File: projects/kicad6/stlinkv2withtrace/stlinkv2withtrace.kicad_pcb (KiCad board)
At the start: 2 copper layers, 7 parts, among them J1 5v jumper, J2 Trace Jumper, J3 STLinkV2, U1 YAAJ_BluePill_Part_Like

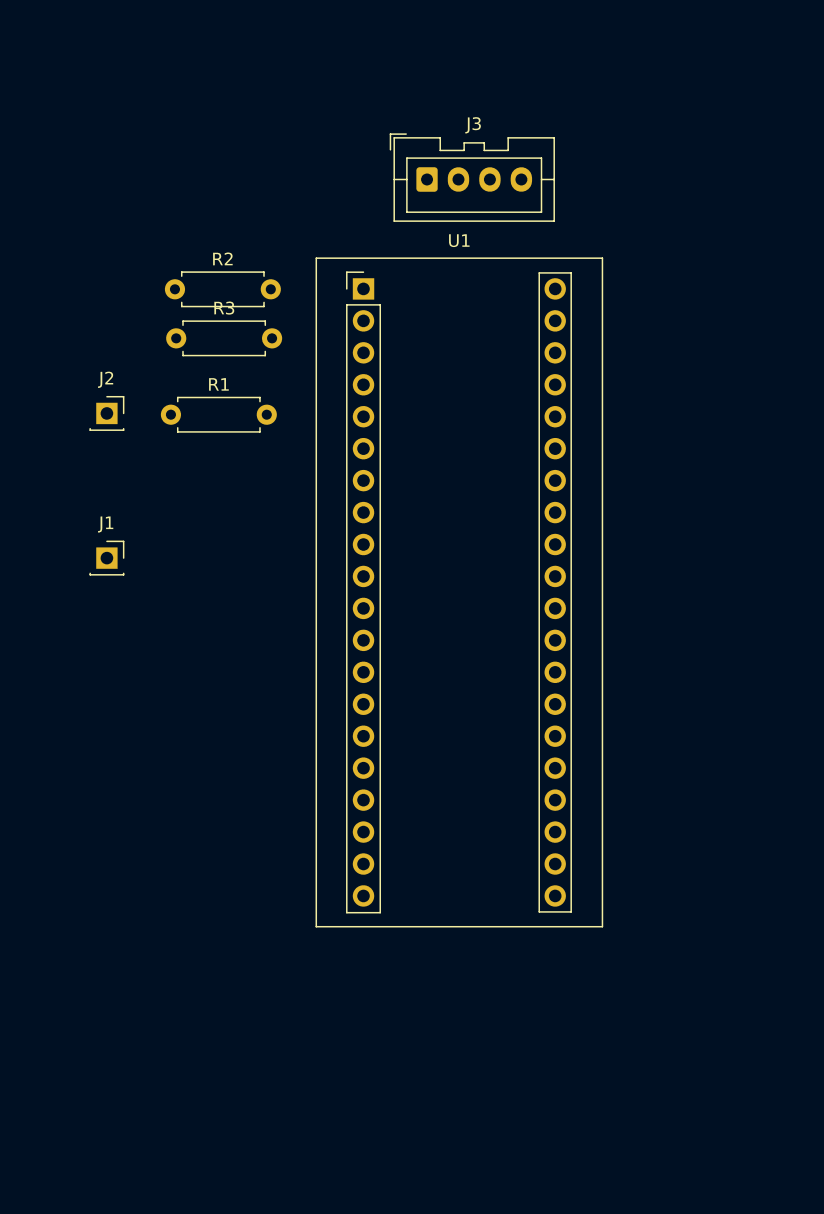
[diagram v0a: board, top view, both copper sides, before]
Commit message: Add stlink v2 diy programmer
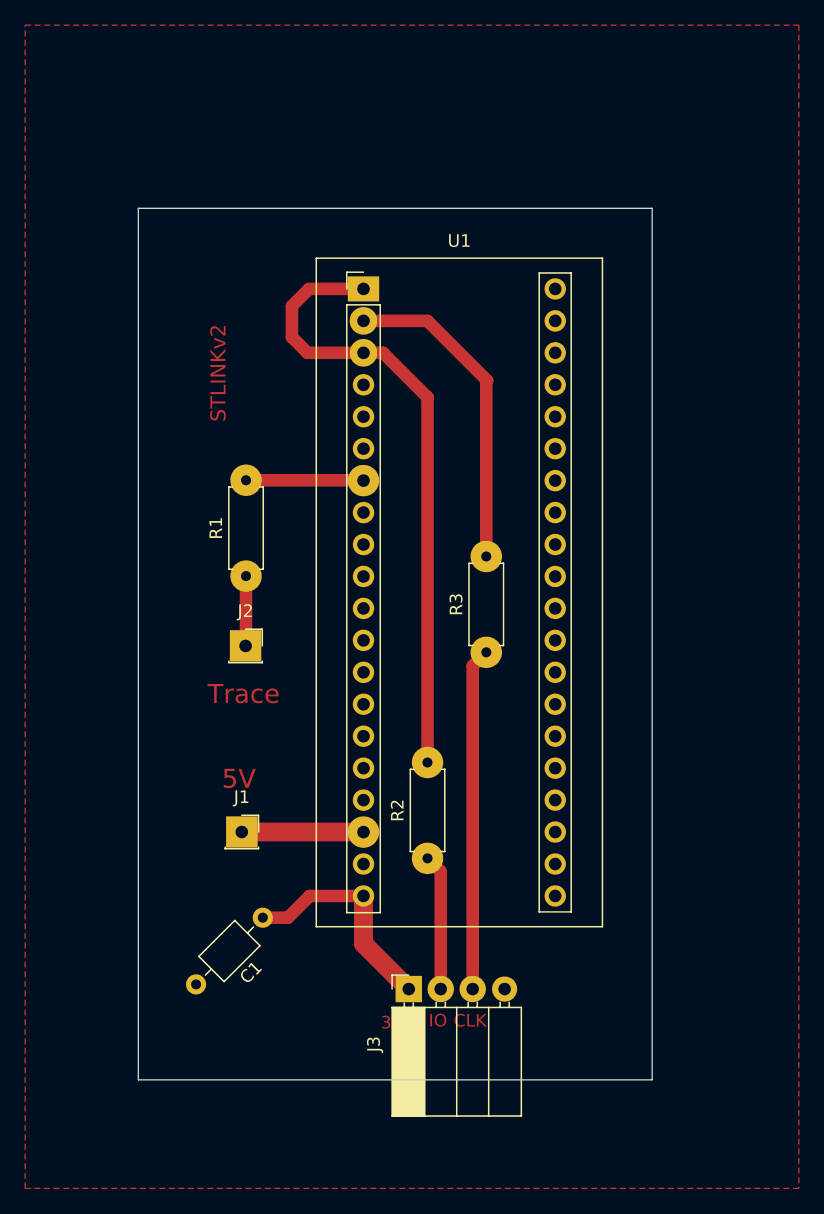
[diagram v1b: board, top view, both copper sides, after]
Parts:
- added C1: 0.1u, Capacitor_THT:C_Axial_L3.8mm_D2.6mm_P7.50mm_Horizontal, F.Cu at (125.0, 121.0)
- J3: footprint Connector_JST:JST_XA_B04B-XASK-1_1x04_P2.50mm_Vertical -> Connector_PinSocket_2.54mm:PinSocket_1x04_P2.54mm_Horizontal
- moved J3 64.4 mm to (136.6, 126.6), turned to 90 degrees
- moved R2 49.5 mm to (138.1, 116.2), turned to 90 degrees
- moved R3 35.1 mm to (142.7, 99.9), turned to 90 degrees
- moved J1 24.3 mm to (123.3, 114.1)
- moved J2 21.5 mm to (123.6, 99.4)
- moved R1 14.2 mm to (123.6, 93.8), turned to 90 degrees
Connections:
- U1 pad 39: unconnected-(U1-Pad39) -> GND
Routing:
- net /IO: track 0.00 -> 50.5 mm
- net Net-(J3-Pad3): track 0.00 -> 27.2 mm
- net /CLK: track 0.00 -> 25.9 mm
- net 3.3V: track 0.00 -> 17.6 mm
- net Net-(J3-Pad2): track 0.00 -> 10.8 mm
- net VCC: track 0.00 -> 9.68 mm
- net /TRACE: track 0.00 -> 9.35 mm
- net Net-(J2-Pad1): track 0.00 -> 5.57 mm
- added copper zone on F.Cu, net GND
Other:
- board outline added: 40.9 x 69.3 mm
- board text added: "3.3V"
- board text added: "5V"
- board text added: "CLK"
- board text added: "IO"
- board text added: "STLINKv2"
- board text added: "Trace"
